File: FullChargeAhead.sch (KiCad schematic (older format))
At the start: 15 parts

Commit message: Did ERC check, annotated
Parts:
- added R107, R108: NOPOP, ~, symbol R
- gave numbers to parts that had none: 15
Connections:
- wire segments 41 -> 46
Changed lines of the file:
@@
 LIBS:FullChargeAhead
 LIBS:CurrentSinkOrSwim
+LIBS:usb-b
+LIBS:FullChargeAhead-cache
 EELAYER 27 0
 EELAYER END
@@
 Sheet 1 1
 Title ""
-Date "27 nov 2015"
+Date "28 nov 2015"
 Rev ""
 Comp ""
@@
 $EndDescr
 $Comp
-L LED D?
+L LED D103
 U 1 1 5658A21A
 P 4000 3450
-F 0 "D?" H 4000 3550 50  0000 C CNN
+F 0 "D103" H 4000 3550 50  0000 C CNN
 F 1 "LED" H 4000 3350 50  0000 C CNN
 F 2 "~" H 4000 3450 60  0000 C CNN
@@
 $EndComp
 $Comp
-L LED D?
+L LED D102
 U 1 1 5658A22D
 P 3650 3450
-F 0 "D?" H 3650 3550 50  0000 C CNN
+F 0 "D102" H 3650 3550 50  0000 C CNN
 F 1 "LED" H 3650 3350 50  0000 C CNN
 F 2 "~" H 3650 3450 60  0000 C CNN
@@
 $EndComp
 $Comp
-L LED D?
+L LED D101
 U 1 1 5658A23A
 P 3350 3450
-F 0 "D?" H 3350 3550 50  0000 C CNN
+F 0 "D101" H 3350 3550 50  0000 C CNN
 F 1 "NOPOP" H 3350 3350 50  0000 C CNN
 F 2 "~" H 3350 3450 60  0000 C CNN
@@
 $EndComp
 $Comp
-L R R?
+L R R101
 U 1 1 5658A242
 P 4450 3750
-F 0 "R?" V 4520 3750 40  0000 C CNN
+F 0 "R101" V 4520 3750 40  0000 C CNN
 F 1 "470" V 4457 3751 40  0000 C CNN
 F 2 "~" V 4380 3750 30  0000 C CNN
@@
 $EndComp
 $Comp
-L R R?
+L R R102
 U 1 1 5658A24F
 P 4450 3900
-F 0 "R?" V 4520 3900 40  0000 C CNN
+F 0 "R102" V 4520 3900 40  0000 C CNN
 F 1 "470" V 4457 3901 40  0000 C CNN
 F 2 "~" V 4380 3900 30  0000 C CNN
@@
 $EndComp
 $Comp
-L R R?
+L R R103
 U 1 1 5658A255
 P 4450 4100
-F 0 "R?" V 4520 4090 40  0000 C CNN
+F 0 "R103" V 4520 4090 40  0000 C CNN
 F 1 "NOPOP" V 4457 4101 40  0000 C CNN
 F 2 "~" V 4380 4100 30  0000 C CNN
@@
 	4700 4100 4900 4100
 $Comp
-L GND #PWR?
+L GND #PWR01
 U 1 1 5658A372
 P 6350 4250
-F 0 "#PWR?" H 6350 4250 30  0001 C CNN
+F 0 "#PWR01" H 6350 4250 30  0001 C CNN
 F 1 "GND" H 6350 4180 30  0001 C CNN
 F 2 "~" H 6350 4250 60  0000 C CNN
@@
 Wire Wire Line
 	7000 4100 6250 4100
-Wire Wire Line
-	6350 4100 6350 4250
-$Comp
-L R R?
+$Comp
+L R R106
 U 1 1 5658A391
 P 6650 3900
-F 0 "R?" V 6550 3900 40  0000 C CNN
+F 0 "R106" V 6550 3900 40  0000 C CNN
 F 1 "2k" V 6657 3901 40  0000 C CNN
 F 2 "~" V 6580 3900 30  0000 C CNN
@@
 Wire Wire Line
 	7000 3900 6900 3900
-Connection ~ 6350 4100
-$Comp
-L R R?
+$Comp
+L R R105
 U 1 1 5658A3CE
 P 6650 3750
-F 0 "R?" V 6730 3750 40  0000 C CNN
+F 0 "R105" V 6730 3750 40  0000 C CNN
 F 1 "10k" V 6657 3751 40  0000 C CNN
 F 2 "~" V 6580 3750 30  0000 C CNN
@@
 	6250 3250 7750 3250
 Wire Wire Line
-	6350 3250 6350 3400
-Wire Wire Line
-	6350 3400 6250 3400
+	6350 3400 6350 3250
 Connection ~ 6350 3250
 $Comp
-L C C?
+L C C102
 U 1 1 5658A458
 P 7200 3500
-F 0 "C?" H 7200 3600 40  0000 L CNN
+F 0 "C102" H 7200 3600 40  0000 L CNN
 F 1 "4.7U" H 7206 3415 40  0000 L CNN
 F 2 "~" H 7238 3350 30  0000 C CNN
@@
 $EndComp
 $Comp
-L GND #PWR?
+L GND #PWR02
 U 1 1 5658A465
 P 7200 3800
-F 0 "#PWR?" H 7200 3800 30  0001 C CNN
+F 0 "#PWR02" H 7200 3800 30  0001 C CNN
 F 1 "GND" H 7200 3730 30  0001 C CNN
 F 2 "~" H 7200 3800 60  0000 C CNN
@@
 Connection ~ 7200 3250
 $Comp
-L CONN_2 P?
+L CONN_2 P102
 U 1 1 5658A4D7
 P 8100 3350
-F 0 "P?" V 8050 3350 40  0000 C CNN
+F 0 "P102" V 8050 3350 40  0000 C CNN
 F 1 "CONN_2" V 8150 3350 40  0000 C CNN
 F 2 "" H 8100 3350 60  0000 C CNN
@@
 Connection ~ 7200 3750
 $Comp
-L C C?
+L C C101
 U 1 1 5658A539
 P 2950 3450
-F 0 "C?" H 2950 3550 40  0000 L CNN
+F 0 "C101" H 2950 3550 40  0000 L CNN
 F 1 "4.7U" H 2956 3365 40  0000 L CNN
 F 2 "~" H 2988 3300 30  0000 C CNN
@@
 Connection ~ 3350 3250
 $Comp
-L USB J?
+L USB J101
 U 1 1 5658A5E9
 P 2190 3050
-F 0 "J?" H 2140 3450 60  0000 C CNN
+F 0 "J101" H 2140 3450 60  0000 C CNN
 F 1 "USB" V 1940 3200 60  0000 C CNN
 F 2 "" H 2190 3050 60  0000 C CNN
@@
 Connection ~ 2950 3250
 $Comp
-L GND #PWR?
+L GND #PWR03
 U 1 1 5658A666
 P 2950 3750
-F 0 "#PWR?" H 2950 3750 30  0001 C CNN
+F 0 "#PWR03" H 2950 3750 30  0001 C CNN
 F 1 "GND" H 2950 3680 30  0001 C CNN
 F 2 "~" H 2950 3750 60  0000 C CNN
@@
 	2950 3650 2950 3750
 $Comp
-L GND #PWR?
+L GND #PWR04
 U 1 1 5658A6D1
 P 2720 3750
-F 0 "#PWR?" H 2720 3750 30  0001 C CNN
+F 0 "#PWR04" H 2720 3750 30  0001 C CNN
 F 1 "GND" H 2720 3680 30  0001 C CNN
 F 2 "~" H 2720 3750 60  0000 C CNN
@@
 	1720 3500 1720 3620
 Wire Wire Line
-	1720 3620 2720 3620
+	1150 3620 2720 3620
 Connection ~ 2720 3620
 $Comp
-L MCP73834-FCI/UN U?
+L MCP73834-FCI/UN U101
 U 1 1 5658A865
 P 5600 3650
-F 0 "U?" H 5600 2950 60  0000 C CNN
+F 0 "U101" H 5600 2950 60  0000 C CNN
 F 1 "MCP73834-FCI/UN" H 5600 4300 60  0000 C CNN
 F 2 "~" H 5550 3350 60  0000 C CNN
@@
 $EndComp
 $Comp
-L R R?
+L R R104
 U 1 1 5658A872
 P 4450 4320
-F 0 "R?" V 4520 4310 40  0000 C CNN
+F 0 "R104" V 4520 4310 40  0000 C CNN
 F 1 "1K" V 4457 4321 40  0000 C CNN
 F 2 "~" V 4380 4320 30  0000 C CNN
@@
 $EndComp
 $Comp
-L CONN_2 P?
+L CONN_2 P101
 U 1 1 5658A882
 P 4480 4650
-F 0 "P?" V 4430 4650 40  0000 C CNN
+F 0 "P101" V 4430 4650 40  0000 C CNN
 F 1 "CONN_2" V 4530 4650 40  0000 C CNN
 F 2 "" H 4480 4650 60  0000 C CNN
@@
 $EndComp
 $Comp
-L GND #PWR?
+L GND #PWR05
 U 1 1 5658A888
 P 4030 4860
-F 0 "#PWR?" H 4030 4860 30  0001 C CNN
+F 0 "#PWR05" H 4030 4860 30  0001 C CNN
 F 1 "GND" H 4030 4790 30  0001 C CNN
 F 2 "~" H 4030 4860 60  0000 C CNN
@@
 	4030 4750 4030 4860
 Wire Wire Line
-	4120 4550 4030 4550
-Wire Wire Line
-	4030 4550 4030 4320
-Wire Wire Line
-	4030 4320 4200 4320
-Wire Wire Line
 	4700 4320 4820 4320
 Wire Wire Line
 	4820 4320 4820 4100
 Connection ~ 4820 4100
+Wire Wire Line
+	4200 4320 4040 4320
+Wire Wire Line
+	4040 4320 4040 4550
+Wire Wire Line
+	4040 4550 4130 4550
+Wire Wire Line
+	6350 4100 6350 4250
+Connection ~ 6350 4100
+Wire Wire Line
+	6250 3400 6350 3400
+$Comp
+L R R107
+U 1 1 5659C14C
+P 1480 3250
+F 0 "R107" V 1550 3240 40  0000 C CNN
+F 1 "NOPOP" V 1487 3251 40  0000 C CNN
+F 2 "~" V 1410 3250 30  0000 C CNN
+F 3 "~" H 1480 3250 30  0000 C CNN
+	1    1480 3250
+	0    -1   -1   0
+$EndComp
+$Comp
+L R R108
+U 1 1 5659C152
+P 1480 3400
+F 0 "R108" V 1550 3390 40  0000 C CNN
+F 1 "NOPOP" V 1487 3401 40  0000 C CNN
+F 2 "~" V 1410 3400 30  0000 C CNN
+F 3 "~" H 1480 3400 30  0000 C CNN
+	1    1480 3400
+	0    -1   -1   0
+$EndComp
+Wire Wire Line
+	1840 3250 1730 3250
+Wire Wire Line
+	1840 3400 1730 3400
+Wire Wire Line
+	1230 3250 1150 3250
+Wire Wire Line
+	1150 3250 1150 3620
+Wire Wire Line
+	1150 3400 1230 3400
+Connection ~ 1720 3620
+Connection ~ 1150 3400
 $EndSCHEMATC

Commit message: Creado footprint del micro USB y el layout
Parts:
- removed J101: USB, symbol USB
- added P103: MICROUSB-B, symbol MICROUSB-B
- added R109: NOPOP, ~, symbol R
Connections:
- wire segments 46 -> 51
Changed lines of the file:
@@
 	3350 4100 4200 4100
 Wire Wire Line
-	2590 3250 4900 3250
+	2480 3250 4900 3250
 Connection ~ 4000 3250
 Connection ~ 3650 3250
@@
 $EndComp
 Connection ~ 3350 3250
-$Comp
-L USB J101
-U 1 1 5658A5E9
-P 2190 3050
-F 0 "J101" H 2140 3450 60  0000 C CNN
-F 1 "USB" V 1940 3200 60  0000 C CNN
-F 2 "" H 2190 3050 60  0000 C CNN
-F 3 "" H 2190 3050 60  0000 C CNN
-	1    2190 3050
-	-1   0    0    -1
-$EndComp
-Connection ~ 2590 3250
 Connection ~ 2950 3250
 $Comp
@@
 	2950 3650 2950 3750
 $Comp
-L GND #PWR04
-U 1 1 5658A6D1
-P 2720 3750
-F 0 "#PWR04" H 2720 3750 30  0001 C CNN
-F 1 "GND" H 2720 3680 30  0001 C CNN
-F 2 "~" H 2720 3750 60  0000 C CNN
-F 3 "~" H 2720 3750 60  0000 C CNN
-	1    2720 3750
-	1    0    0    -1
-$EndComp
-Wire Wire Line
-	2590 3400 2720 3400
-Wire Wire Line
-	2720 3400 2720 3750
-Wire Wire Line
-	2590 3500 2720 3500
-Connection ~ 2720 3500
-Wire Wire Line
-	1840 3500 1720 3500
-Wire Wire Line
-	1720 3500 1720 3620
-Wire Wire Line
-	1150 3620 2720 3620
-Connection ~ 2720 3620
-$Comp
 L MCP73834-FCI/UN U101
 U 1 1 5658A865
@@
 $EndComp
 $Comp
-L GND #PWR05
+L GND #PWR04
 U 1 1 5658A888
 P 4030 4860
-F 0 "#PWR05" H 4030 4860 30  0001 C CNN
+F 0 "#PWR04" H 4030 4860 30  0001 C CNN
 F 1 "GND" H 4030 4790 30  0001 C CNN
 F 2 "~" H 4030 4860 60  0000 C CNN
@@
 	6250 3400 6350 3400
 $Comp
+L GND #PWR05
+U 1 1 5659D574
+P 2920 2560
+F 0 "#PWR05" H 2920 2560 30  0001 C CNN
+F 1 "GND" H 2920 2490 30  0001 C CNN
+F 2 "~" H 2920 2560 60  0000 C CNN
+F 3 "~" H 2920 2560 60  0000 C CNN
+	1    2920 2560
+	1    0    0    -1
+$EndComp
+Wire Wire Line
+	880  3200 1080 3200
+Wire Wire Line
+	880  2420 880  3200
+Wire Wire Line
+	880  2420 3220 2420
+Wire Wire Line
+	2920 2420 2920 2560
+Wire Wire Line
+	2480 2850 2620 2850
+Wire Wire Line
+	2620 2850 2620 2420
+Connection ~ 2620 2420
+Wire Wire Line
+	1080 2900 880  2900
+Connection ~ 880  2900
+Wire Wire Line
+	1080 3000 880  3000
+Connection ~ 880  3000
+Wire Wire Line
+	1080 3100 880  3100
+Connection ~ 880  3100
+$Comp
 L R R107
-U 1 1 5659C14C
-P 1480 3250
-F 0 "R107" V 1550 3240 40  0000 C CNN
-F 1 "NOPOP" V 1487 3251 40  0000 C CNN
-F 2 "~" V 1410 3250 30  0000 C CNN
-F 3 "~" H 1480 3250 30  0000 C CNN
-	1    1480 3250
+U 1 1 5659D6A2
+P 2870 2950
+F 0 "R107" V 2940 2940 40  0000 C CNN
+F 1 "NOPOP" V 2877 2951 40  0000 C CNN
+F 2 "~" V 2800 2950 30  0000 C CNN
+F 3 "~" H 2870 2950 30  0000 C CNN
+	1    2870 2950
 	0    -1   -1   0
 $EndComp
 $Comp
 L R R108
-U 1 1 5659C152
-P 1480 3400
-F 0 "R108" V 1550 3390 40  0000 C CNN
-F 1 "NOPOP" V 1487 3401 40  0000 C CNN
-F 2 "~" V 1410 3400 30  0000 C CNN
-F 3 "~" H 1480 3400 30  0000 C CNN
-	1    1480 3400
-	0    -1   -1   0
-$EndComp
-Wire Wire Line
-	1840 3250 1730 3250
-Wire Wire Line
-	1840 3400 1730 3400
-Wire Wire Line
-	1230 3250 1150 3250
-Wire Wire Line
-	1150 3250 1150 3620
-Wire Wire Line
-	1150 3400 1230 3400
-Connection ~ 1720 3620
-Connection ~ 1150 3400
+U 1 1 5659D6A8
+P 2870 3050
+F 0 "R108" V 2940 3040 40  0000 C CNN
+F 1 "NOPOP" V 2877 3051 40  0000 C CNN
+F 2 "~" V 2800 3050 30  0000 C CNN
+F 3 "~" H 2870 3050 30  0000 C CNN
+	1    2870 3050
+	0    -1   -1   0
+$EndComp
+$Comp
+L R R109
+U 1 1 5659D6AE
+P 2870 3150
+F 0 "R109" V 2940 3140 40  0000 C CNN
+F 1 "NOPOP" V 2877 3151 40  0000 C CNN
+F 2 "~" V 2800 3150 30  0000 C CNN
+F 3 "~" H 2870 3150 30  0000 C CNN
+	1    2870 3150
+	0    -1   -1   0
+$EndComp
+Wire Wire Line
+	2480 2950 2620 2950
+Wire Wire Line
+	2620 3050 2480 3050
+Wire Wire Line
+	2480 3150 2620 3150
+Wire Wire Line
+	3120 2950 3220 2950
+Wire Wire Line
+	3220 2420 3220 3150
+Connection ~ 2920 2420
+Wire Wire Line
+	3220 3150 3120 3150
+Connection ~ 3220 2950
+Wire Wire Line
+	3120 3050 3220 3050
+Connection ~ 3220 3050
+$Comp
+L MICROUSB-B P103
+U 1 1 5659D9B5
+P 1780 3050
+F 0 "P103" H 2080 2650 60  0000 C CNN
+F 1 "MICROUSB-B" H 1780 3400 60  0000 C CNN
+F 2 "" H 2180 2850 60  0000 C CNN
+F 3 "" H 2180 2850 60  0000 C CNN
+	1    1780 3050
+	1    0    0    -1
+$EndComp
 $EndSCHEMATC

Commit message: Seguimos con el layout
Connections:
- net Vdd: now reaches C101.1, D101.1 (A), D102.1 (A), D103.1 (A), P103.1 (VBUS), U101.1 (Vdd), U101.2 (Vdd)
- net Vbat: now reaches C102.1, P102.1 (P1), U101.10 (Vbat), U101.9 (Vbat)
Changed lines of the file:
@@
 Sheet 1 1
 Title ""
-Date "28 nov 2015"
+Date "29 nov 2015"
 Rev ""
 Comp ""
@@
 	1    0    0    -1
 $EndComp
+Text Label 4250 3250 0    60   ~ 0
+Vdd
+Text Label 6650 3250 0    60   ~ 0
+Vbat
 $EndSCHEMATC

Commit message: Finalizando el layout
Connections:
- net GND: no longer R107.2, R108.2, R109.2
- net Vdd: now also R107.2, R108.2, R109.2
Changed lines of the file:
@@
 Sheet 1 1
 Title ""
-Date "29 nov 2015"
+Date "2 dec 2015"
 Rev ""
 Comp ""
@@
 	880  2420 880  3200
 Wire Wire Line
-	880  2420 3220 2420
-Wire Wire Line
 	2920 2420 2920 2560
 Wire Wire Line
 	2480 2850 2620 2850
-Wire Wire Line
-	2620 2850 2620 2420
-Connection ~ 2620 2420
 Wire Wire Line
 	1080 2900 880  2900
@@
 	3120 2950 3220 2950
 Wire Wire Line
-	3220 2420 3220 3150
-Connection ~ 2920 2420
-Wire Wire Line
 	3220 3150 3120 3150
-Connection ~ 3220 2950
-Wire Wire Line
-	3120 3050 3220 3050
-Connection ~ 3220 3050
 $Comp
 L MICROUSB-B P103
@@
 Text Label 6650 3250 0    60   ~ 0
 Vbat
+Wire Wire Line
+	880  2420 2920 2420
+Wire Wire Line
+	2620 2850 2620 2420
+Connection ~ 2620 2420
+Wire Wire Line
+	3220 2950 3220 3250
+Connection ~ 3220 3250
+Connection ~ 3220 3150
+Wire Wire Line
+	3120 3050 3220 3050
+Connection ~ 3220 3050
 $EndSCHEMATC

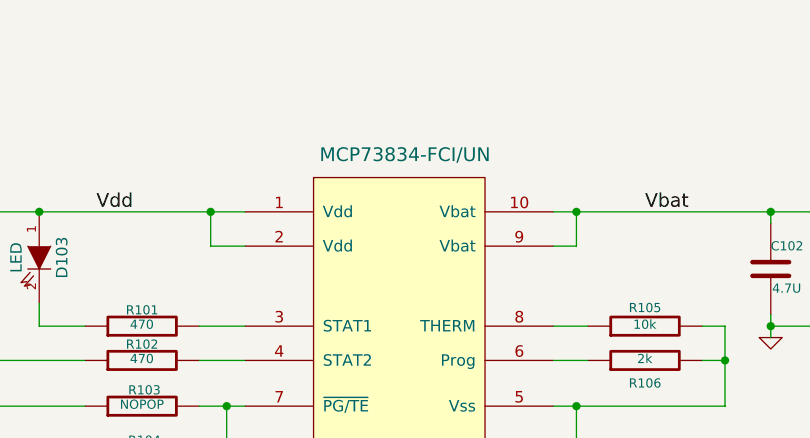
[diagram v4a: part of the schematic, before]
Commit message: Creada una primera versión del BOM
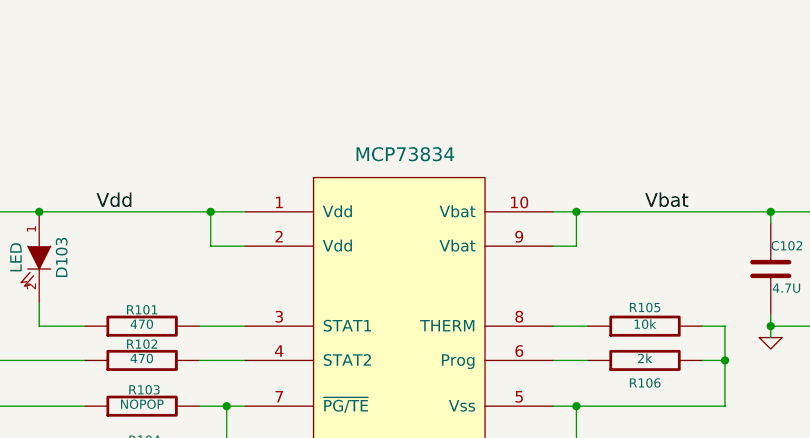
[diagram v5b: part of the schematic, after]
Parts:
- P103: MFG Name (none) -> 10103594-0001LF
- U101: value MCP73834-FCI/UN -> MCP73834; MFG Name (none) -> MCP73834-FCI/UN
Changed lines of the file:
@@
 Sheet 1 1
 Title ""
-Date "2 dec 2015"
+Date "7 dec 2015"
 Rev ""
 Comp ""
@@
 P 5600 3650
 F 0 "U101" H 5600 2950 60  0000 C CNN
-F 1 "MCP73834-FCI/UN" H 5600 4300 60  0000 C CNN
+F 1 "MCP73834" H 5600 4300 60  0000 C CNN
 F 2 "~" H 5550 3350 60  0000 C CNN
 F 3 "~" H 5550 3350 60  0000 C CNN
+F 4 "MCP73834-FCI/UN" H 5600 3650 60  0001 C CNN "MFG Name"
 	1    5600 3650
 	1    0    0    -1
@@
 F 2 "" H 2180 2850 60  0000 C CNN
 F 3 "" H 2180 2850 60  0000 C CNN
+F 4 "10103594-0001LF" H 1780 3050 60  0001 C CNN "MFG Name"
 	1    1780 3050
 	1    0    0    -1
